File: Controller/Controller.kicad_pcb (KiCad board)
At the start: 2 copper layers, 132 x 70 mm, 16 parts, among them J1 Probe, J2 Sonde, J3 Power, J4 D_Connector, J5 HayRain 3 Way, J6 SCT013, K1 FINDER-36.11, Q1 BC337, U4 TSR_1-2433

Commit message: Changed Readme, Bumped Version
Changed version/Revision to 1.0
Fixed MQTT_ID
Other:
- board text added: "${REVISION}"
- board text added: "Version"
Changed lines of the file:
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@@
 	(paper "A4")
 	(title_block
-		(title "24V")
+		(title "24V, SCT033 Vertical")
 		(date "2025-05-12")
 		(rev "1.0")
@@
 		)
 	)
+	(property "VERSION" "1.0")
 	(net 0 "")
 	(net 1 "SCL")
@@
 		)
 	)
+	(gr_text "Version"
+		(at 100.5 67.75 0)
+		(layer "Dwgs.User")
+		(effects
+			(font
+				(size 1.5 1.5)
+				(thickness 0.3)
+				(bold yes)
+			)
+			(justify left bottom)
+		)
+	)
+	(gr_text "${REVISION}"
+		(at 110.5 67.75 0)
+		(layer "Dwgs.User")
+		(effects
+			(font
+				(size 1.5 1.5)
+				(thickness 0.3)
+				(bold yes)
+			)
+			(justify left bottom)
+		)
+	)
 	(segment
 		(start 200.45 88.8475)
@@
 		(min_thickness 0.25)
 		(filled_areas_thickness no)
-		(fill yes
+		(fill
 			(thermal_gap 0.5)
 			(thermal_bridge_width 0.5)
@@
 		(min_thickness 0.25)
 		(filled_areas_thickness no)
-		(fill yes
+		(fill
 			(thermal_gap 0.5)
 			(thermal_bridge_width 0.5)
@@
 	)
 	(group ""
+		(members "223312d3-71f6-4376-98c8-30cf0bb321c3" "40566afd-9096-4068-93d2-571bdf5ada37")
+	)
+	(group ""

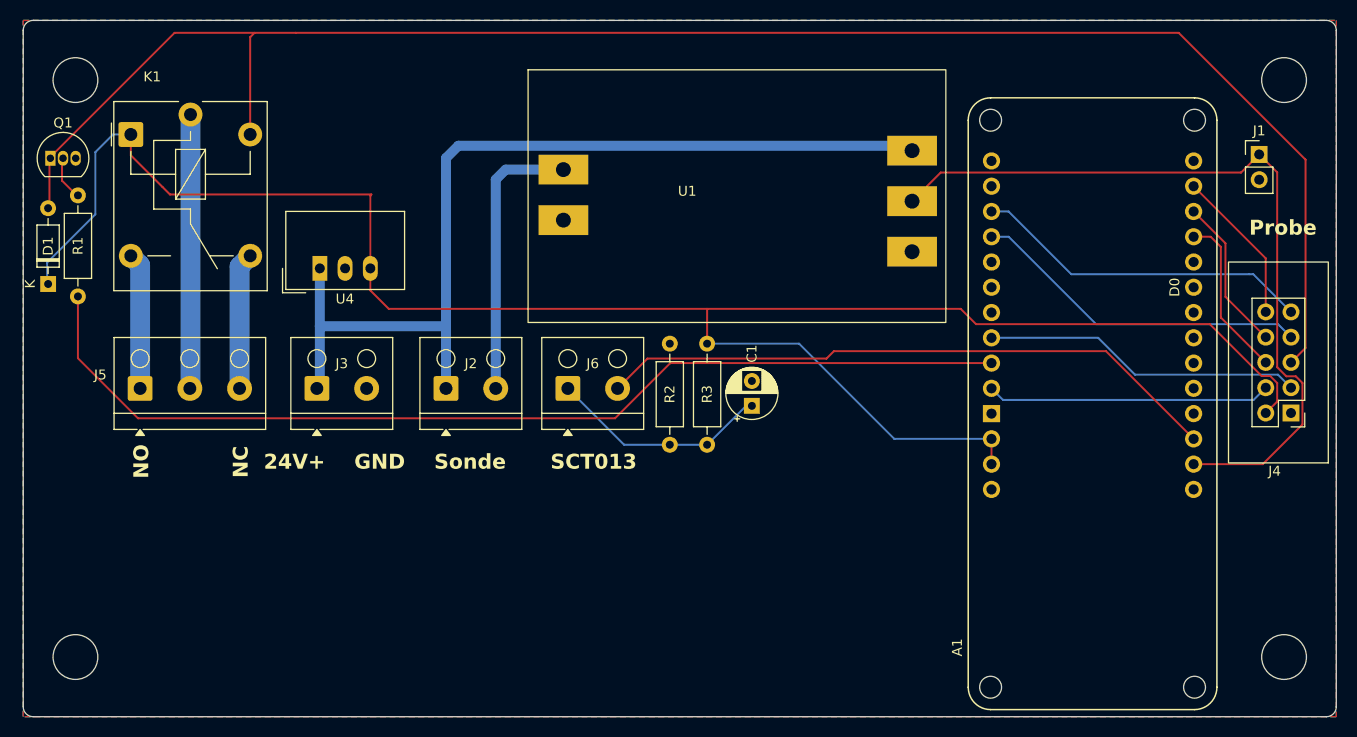
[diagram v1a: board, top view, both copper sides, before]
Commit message: Footprints updated, AREF to VCC
Updated Footprints from updatet Libraries and connected AREF to VCC,
Rerouted
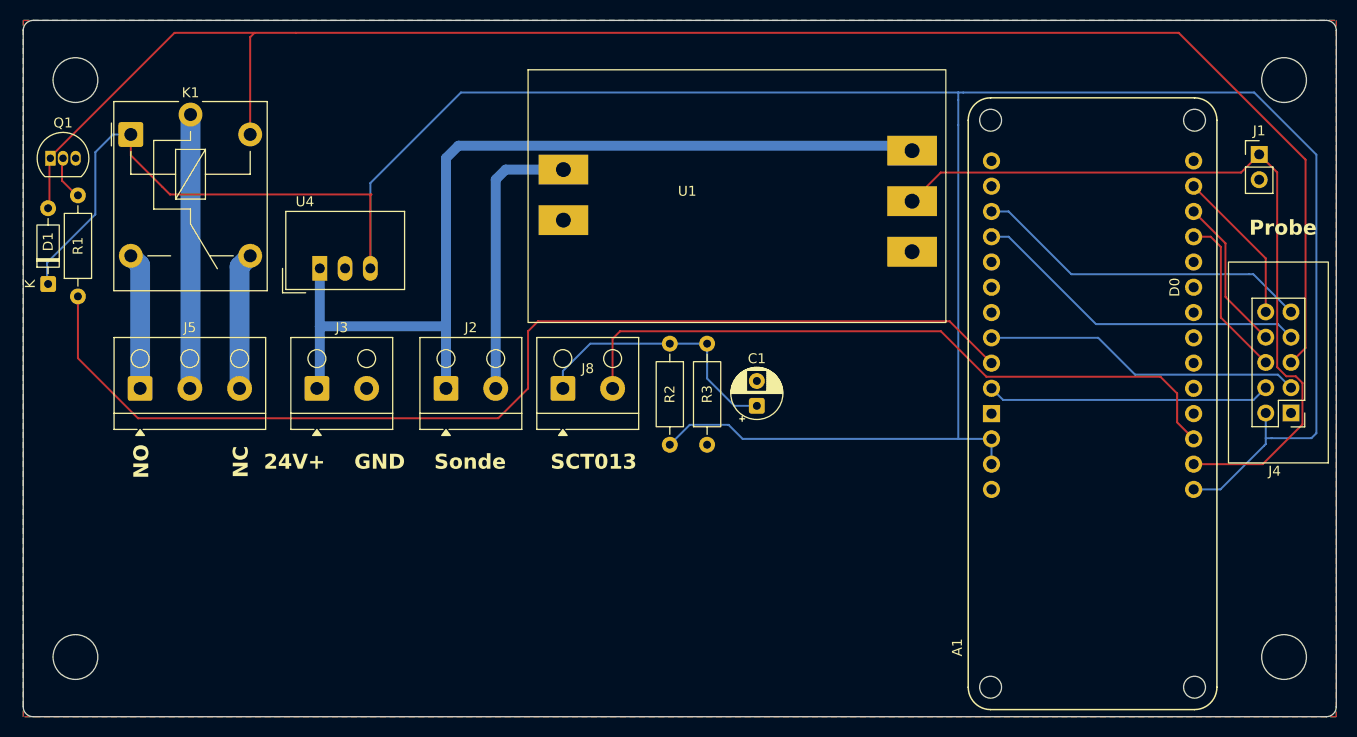
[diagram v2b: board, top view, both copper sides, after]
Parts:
- removed J6: SCT013, TerminalBlock_RND:TerminalBlock_RND_205-00001_1x02_P5.00mm_Horizontal
- added J8: SCT013, TerminalBlock_RND:TerminalBlock_RND_205-00001_1x02_P5.00mm_Horizontal, F.Cu at (127.2, 94.0)
- moved C1 0.50 mm to (146.8, 95.8)
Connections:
- A1 pad AREF: unconnected-(A1-PadAREF) -> VCC
- R2 pad 1: GND -> /L
- R2 pad 2: /L -> VCC
- R3 pad 1: /L -> GND
- R3 pad 2: VCC -> /L
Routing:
- net VCC: track 195.1 -> 282.5 mm
- net VALVE: track 102.9 -> 109.7 mm
- net /K: track 63.1 -> 69.9 mm
- net /L: track 22.5 -> 27.0 mm
